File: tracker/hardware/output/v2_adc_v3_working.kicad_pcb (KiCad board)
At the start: 2 copper layers, 50 x 40 mm, 17 parts, among them U1 ESP32-C3, U2 LR2021F33, U3 MAX-M10S, U4 TPS7A02

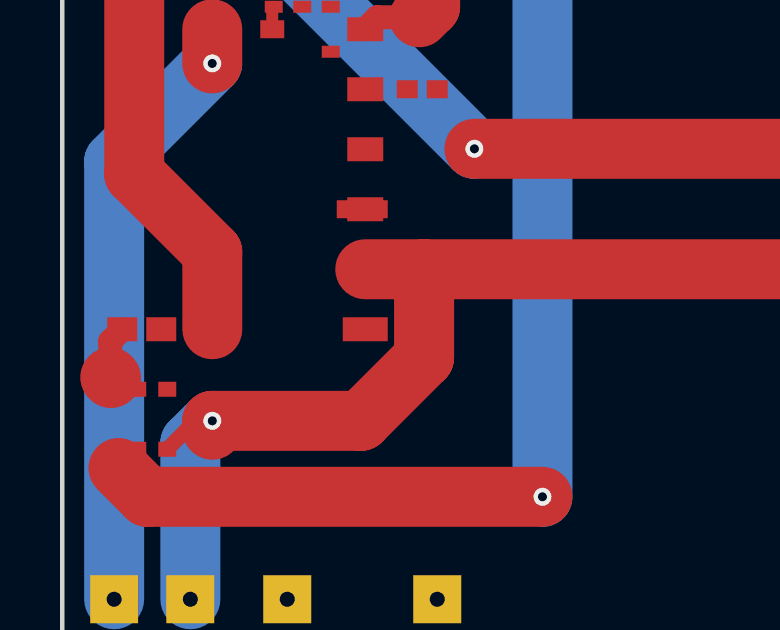
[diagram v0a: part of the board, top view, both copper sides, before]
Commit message: persist: kimi-k3 power routing scripts + inspection tools (2-layer power routing abandoned — needs 4-layer)
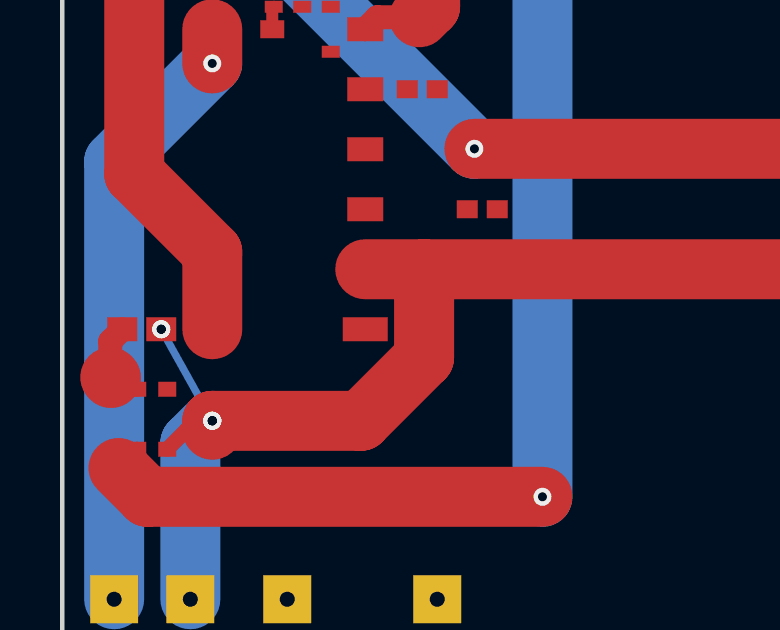
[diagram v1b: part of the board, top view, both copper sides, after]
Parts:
- moved C2 4.00 mm to (14.0, 24.0)
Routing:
- net GND: track 83.1 -> 86.6 mm, vias 1 -> 5
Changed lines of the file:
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@@
 	(footprint ""
 		(layer "F.Cu")
-		(at 10 24)
+		(at 14 24)
 		(property "Reference" "C2"
 			(at 0 0 0)
@@
 	)
 	(via
+		(at 3.3 28)
+		(size 0.6)
+		(drill 0.3)
+		(layers "F.Cu" "B.Cu")
+		(net 2)
+	)
+	(via
+		(at 3.3 28)
+		(size 0.6)
+		(drill 0.3)
+		(layers "F.Cu" "B.Cu")
+		(net 2)
+	)
+	(via
+		(at 5 31.05)
+		(size 0.6)
+		(drill 0.3)
+		(layers "F.Cu" "B.Cu")
+		(net 2)
+	)
+	(via
 		(at 5.0019 31.0531)
 		(size 0.6)
@@
 		(net 2)
 	)
+	(via
+		(at 5 31.05)
+		(size 0.6)
+		(drill 0.3)
+		(layers "F.Cu" "B.Cu")
+		(net 2)
+	)
 	(segment
 		(start 4.27 37)
@@
 		(layer "B.Cu")
 		(net 2)
+	)
+	(segment
+		(start 3.3 28)
+		(end 5 31.05)
+		(width 0.25)
+		(layer "B.Cu")
+		(net 2)

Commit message: wip: persist kimi-k3 partial work — 8th timeout on delegate_task (300s limit)
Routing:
- net GND: vias 5 -> 1
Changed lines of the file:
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@@
-	)
-	(via
-		(at 3.3 28)
-		(size 0.6)
-		(drill 0.3)
-		(layers "F.Cu" "B.Cu")
-		(net 2)
-	)
-	(via
-		(at 3.3 28)
-		(size 0.6)
-		(drill 0.3)
-		(layers "F.Cu" "B.Cu")
-		(net 2)
-	)
-	(via
-		(at 5 31.05)
-		(size 0.6)
-		(drill 0.3)
-		(layers "F.Cu" "B.Cu")
-		(net 2)
 	)
 	(via
@@
 		(size 0.6)
 		(drill 0.3)
-		(layers "F.Cu" "B.Cu")
-		(net 2)
-	)
-	(via
-		(at 5 31.05)
-		(size 0.6)
-		(drill 0.3)

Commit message: wip: commit all PCB work — 4layer scripts, routing outputs, DSN/SES files
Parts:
- moved C2 2.83 mm to (12.0, 22.0)
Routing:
- net GND: vias 1 -> 2
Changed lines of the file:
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@@
 	(footprint ""
 		(layer "F.Cu")
-		(at 14 24)
+		(at 12 22)
 		(property "Reference" "C2"
 			(at 0 0 0)
@@
 	)
 	(via
+		(at 3.3 28)
+		(size 0.6)
+		(drill 0.3)
+		(layers "F.Cu" "B.Cu")
+		(net 2)
+	)
+	(via
 		(at 5.0019 31.0531)
 		(size 0.6)
@@
 		(start 3.3 28)
 		(end 5 31.05)
-		(width 0.25)
+		(width 0.3)
 		(layer "B.Cu")
 		(net 2)
